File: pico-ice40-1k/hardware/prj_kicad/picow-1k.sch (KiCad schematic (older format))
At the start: 4 parts, among them U1 ICE40HX1K-TQ144, X1 OSC

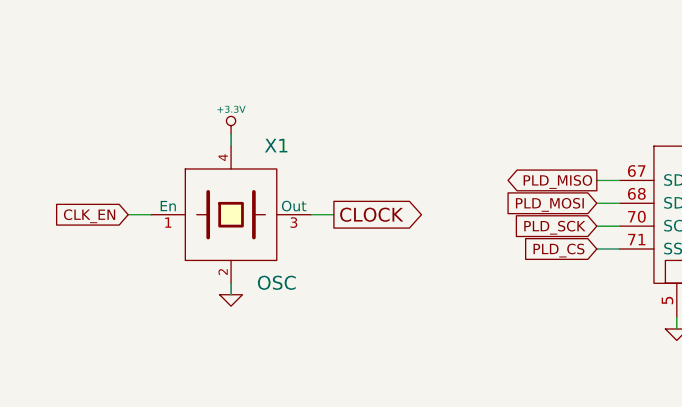
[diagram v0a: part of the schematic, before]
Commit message: = UPD: Update hardware for rev 0.2.1 board (mainly bugfix)
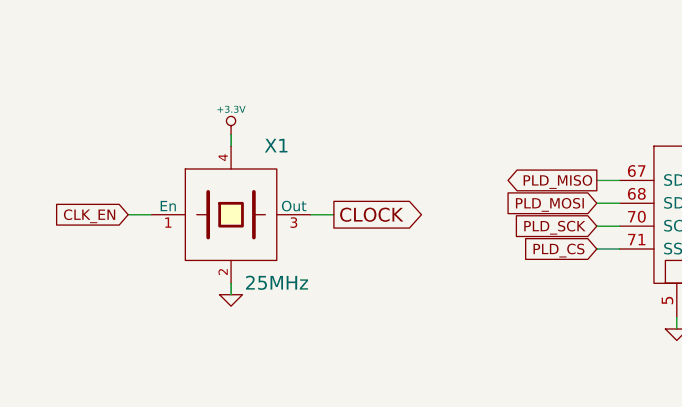
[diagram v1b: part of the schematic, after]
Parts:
- X1: value OSC -> 25MHz; Manuf Ref (none) -> 501JAA25M0000BAF; Manufacturer (none) -> Silicon Labs
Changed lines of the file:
@@
 P 1500 6550
 F 0 "X1" H 1700 6850 60  0000 C CNN
-F 1 "OSC" H 1700 6250 60  0000 C CNN
+F 1 "25MHz" H 1700 6250 60  0000 C CNN
 F 2 "" H 1500 6550 60  0000 C CNN
 F 3 "" H 1500 6550 60  0000 C CNN
+F 4 "Silicon Labs" H 1500 6550 60  0001 C CNN "Manufacturer"
+F 5 "501JAA25M0000BAF" H 1500 6550 60  0001 C CNN "Manuf Ref"
 	1    1500 6550
 	1    0    0    -1
